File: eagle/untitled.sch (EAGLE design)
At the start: 42 parts, among them J1 JTAG, Q1 16MHz, U1 MMA3202KEG

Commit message: Update board layout.
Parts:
- added D9: (no value), SparkFun-LED:LED1206
- added JP3: (no value), SparkFun-Connectors:M04PTH
- added R14: (no value), SparkFun-Passives:RESISTOR1206
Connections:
- new net N$18: D9.A, R14.2
- new net PB0: JP3.3, U$1.PB0(SS)
- new net PD0: JP3.1, U$1.PD0(SCL)
- new net PD1: JP3.2, U$1.PD1(SDA)
- new net PE6: JP3.4, U$1.PE6
- net GND-ISO: now also D9.C
- net N$28: now also R14.1
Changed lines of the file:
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@@
 <part name="D11" library="gipi" deviceset="DIODE" device=""/>
 <part name="D12" library="gipi" deviceset="DIODE" device=""/>
+<part name="D9" library="SparkFun-LED" deviceset="LED" device="1206"/>
+<part name="R14" library="SparkFun-Passives" deviceset="RESISTOR" device="1206"/>
+<part name="GND-ISO11" library="SparkFun-Aesthetics" deviceset="GND-ISO" device=""/>
+<part name="JP3" library="SparkFun-Connectors" deviceset="M04" device="PTH"/>
 </parts>
 <sheets>
@@
 <instance part="D11" gate="G$1" x="-35.56" y="88.9"/>
 <instance part="D12" gate="G$1" x="185.42" y="40.64"/>
+<instance part="D9" gate="G$1" x="-27.94" y="104.14" rot="R90"/>
+<instance part="R14" gate="G$1" x="-30.48" y="96.52" rot="R90"/>
+<instance part="GND-ISO11" gate="G$1" x="-22.86" y="93.98"/>
+<instance part="JP3" gate="G$1" x="-33.02" y="-40.64"/>
 </instances>
 <busses>
@@
 <pinref part="GND-ISO10" gate="G$1" pin="GND-ISO"/>
 </segment>
+<segment>
+<pinref part="D9" gate="G$1" pin="C"/>
+<wire x1="-22.86" y1="104.14" x2="-22.86" y2="96.52" width="0.1524" layer="91"/>
+<pinref part="GND-ISO11" gate="G$1" pin="GND-ISO"/>
+</segment>
 </net>
 <net name="N$19" class="0">
@@
 <wire x1="-33.02" y1="88.9" x2="-30.48" y2="88.9" width="0.1524" layer="91"/>
 <junction x="-30.48" y="88.9"/>
+<pinref part="R14" gate="G$1" pin="1"/>
+<wire x1="-30.48" y1="88.9" x2="-30.48" y2="91.44" width="0.1524" layer="91"/>
 </segment>
 </net>
@@
 </segment>
 </net>
+<net name="N$18" class="0">
+<segment>
+<pinref part="R14" gate="G$1" pin="2"/>
+<pinref part="D9" gate="G$1" pin="A"/>
+<wire x1="-30.48" y1="101.6" x2="-30.48" y2="104.14" width="0.1524" layer="91"/>
+</segment>
+</net>
+<net name="PB0" class="0">
+<segment>
+<pinref part="U$1" gate="G$1" pin="PB0(SS)"/>
+<wire x1="60.96" y1="20.32" x2="71.12" y2="20.32" width="0.1524" layer="91"/>
+<label x="73.66" y="20.32" size="1.778" layer="95" xref="yes"/>
+</segment>
+<segment>
+<pinref part="JP3" gate="G$1" pin="3"/>
+<wire x1="-27.94" y1="-38.1" x2="-22.86" y2="-38.1" width="0.1524" layer="91"/>
+<label x="-22.86" y="-38.1" size="1.778" layer="95" xref="yes"/>
+</segment>
+</net>
+<net name="PE6" class="0">
+<segment>
+<pinref part="U$1" gate="G$1" pin="PE6"/>
+<wire x1="60.96" y1="38.1" x2="71.12" y2="38.1" width="0.1524" layer="91"/>
+<label x="73.66" y="38.1" size="1.778" layer="95" xref="yes"/>
+</segment>
+<segment>
+<pinref part="JP3" gate="G$1" pin="4"/>
+<wire x1="-27.94" y1="-35.56" x2="-22.86" y2="-35.56" width="0.1524" layer="91"/>
+<label x="-22.86" y="-35.56" size="1.778" layer="95" xref="yes"/>
+</segment>
+</net>
+<net name="PD0" class="0">
+<segment>
+<pinref part="U$1" gate="G$1" pin="PD0(SCL)"/>
+<wire x1="60.96" y1="48.26" x2="71.12" y2="48.26" width="0.1524" layer="91"/>
+<label x="73.66" y="48.26" size="1.778" layer="95" xref="yes"/>
+</segment>
+<segment>
+<pinref part="JP3" gate="G$1" pin="1"/>
+<wire x1="-27.94" y1="-43.18" x2="-22.86" y2="-43.18" width="0.1524" layer="91"/>
+<label x="-22.86" y="-43.18" size="1.778" layer="95" xref="yes"/>
+</segment>
+</net>
+<net name="PD1" class="0">
+<segment>
+<pinref part="U$1" gate="G$1" pin="PD1(SDA)"/>
+<wire x1="60.96" y1="50.8" x2="71.12" y2="50.8" width="0.1524" layer="91"/>
+<label x="73.66" y="50.8" size="1.778" layer="95" xref="yes"/>
+</segment>
+<segment>
+<pinref part="JP3" gate="G$1" pin="2"/>
+<wire x1="-27.94" y1="-40.64" x2="-22.86" y2="-40.64" width="0.1524" layer="91"/>
+<label x="-22.86" y="-40.64" size="1.778" layer="95" xref="yes"/>
+</segment>
+</net>

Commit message: Update eagle.
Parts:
- added U$2: KITTEN, gipi:KITTEN
- G1: device battery:10MM_SM_COIN_CELL_CLIP -> SparkFun-Electromechanical:BATTERY20PTH
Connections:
- net GND-ISO: now also G1.+; no longer G1.-
- net N$33: now also G1.-; no longer G1.+
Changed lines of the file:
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@@
 <part name="C2" library="SparkFun-Capacitors" deviceset="CAP" device="1206"/>
 <part name="U1" library="gipi" deviceset="MMA3202KEG" device=""/>
-<part name="G1" library="battery" deviceset="10MM_SM_COIN_CELL_CLIP" device="" value="BAT"/>
+<part name="G1" library="SparkFun-Electromechanical" deviceset="BATTERY" device="20PTH" value="BAT"/>
 <part name="GND-ISO4" library="SparkFun-Aesthetics" deviceset="GND-ISO" device=""/>
 <part name="C3" library="SparkFun-Capacitors" deviceset="CAP" device="1206"/>
@@
 <part name="GND-ISO11" library="SparkFun-Aesthetics" deviceset="GND-ISO" device=""/>
 <part name="JP3" library="SparkFun-Connectors" deviceset="M04" device="PTH"/>
+<part name="U$2" library="gipi" deviceset="KITTEN" device=""/>
 </parts>
 <sheets>
@@
 </segment>
 <segment>
-<pinref part="G1" gate="G$1" pin="-"/>
+<pinref part="G1" gate="G$1" pin="+"/>
 <wire x1="-40.64" y1="78.74" x2="-40.64" y2="68.58" width="0.1524" layer="91"/>
 <pinref part="GND-ISO5" gate="G$1" pin="GND-ISO"/>
@@
 <net name="N$33" class="0">
 <segment>
-<pinref part="G1" gate="G$1" pin="+"/>
+<pinref part="G1" gate="G$1" pin="-"/>
 <pinref part="D11" gate="G$1" pin="A"/>
 <wire x1="-40.64" y1="88.9" x2="-38.1" y2="88.9" width="0.1524" layer="91"/>

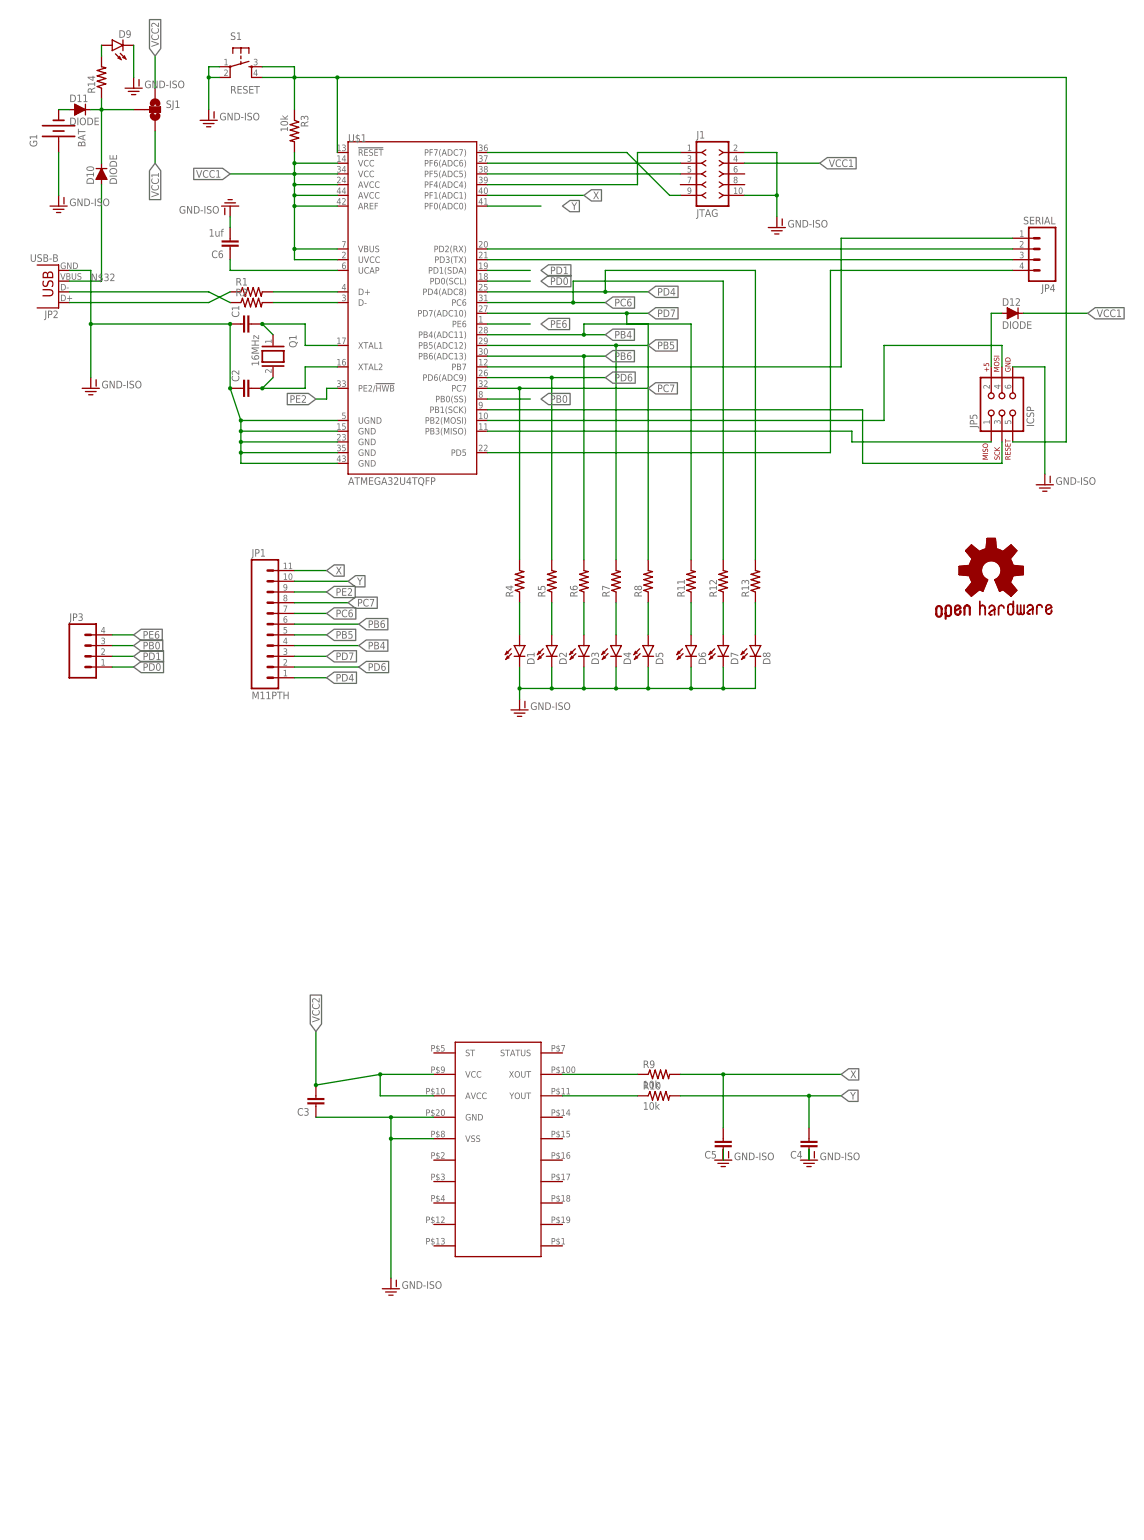
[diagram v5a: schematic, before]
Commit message: Update some component values.
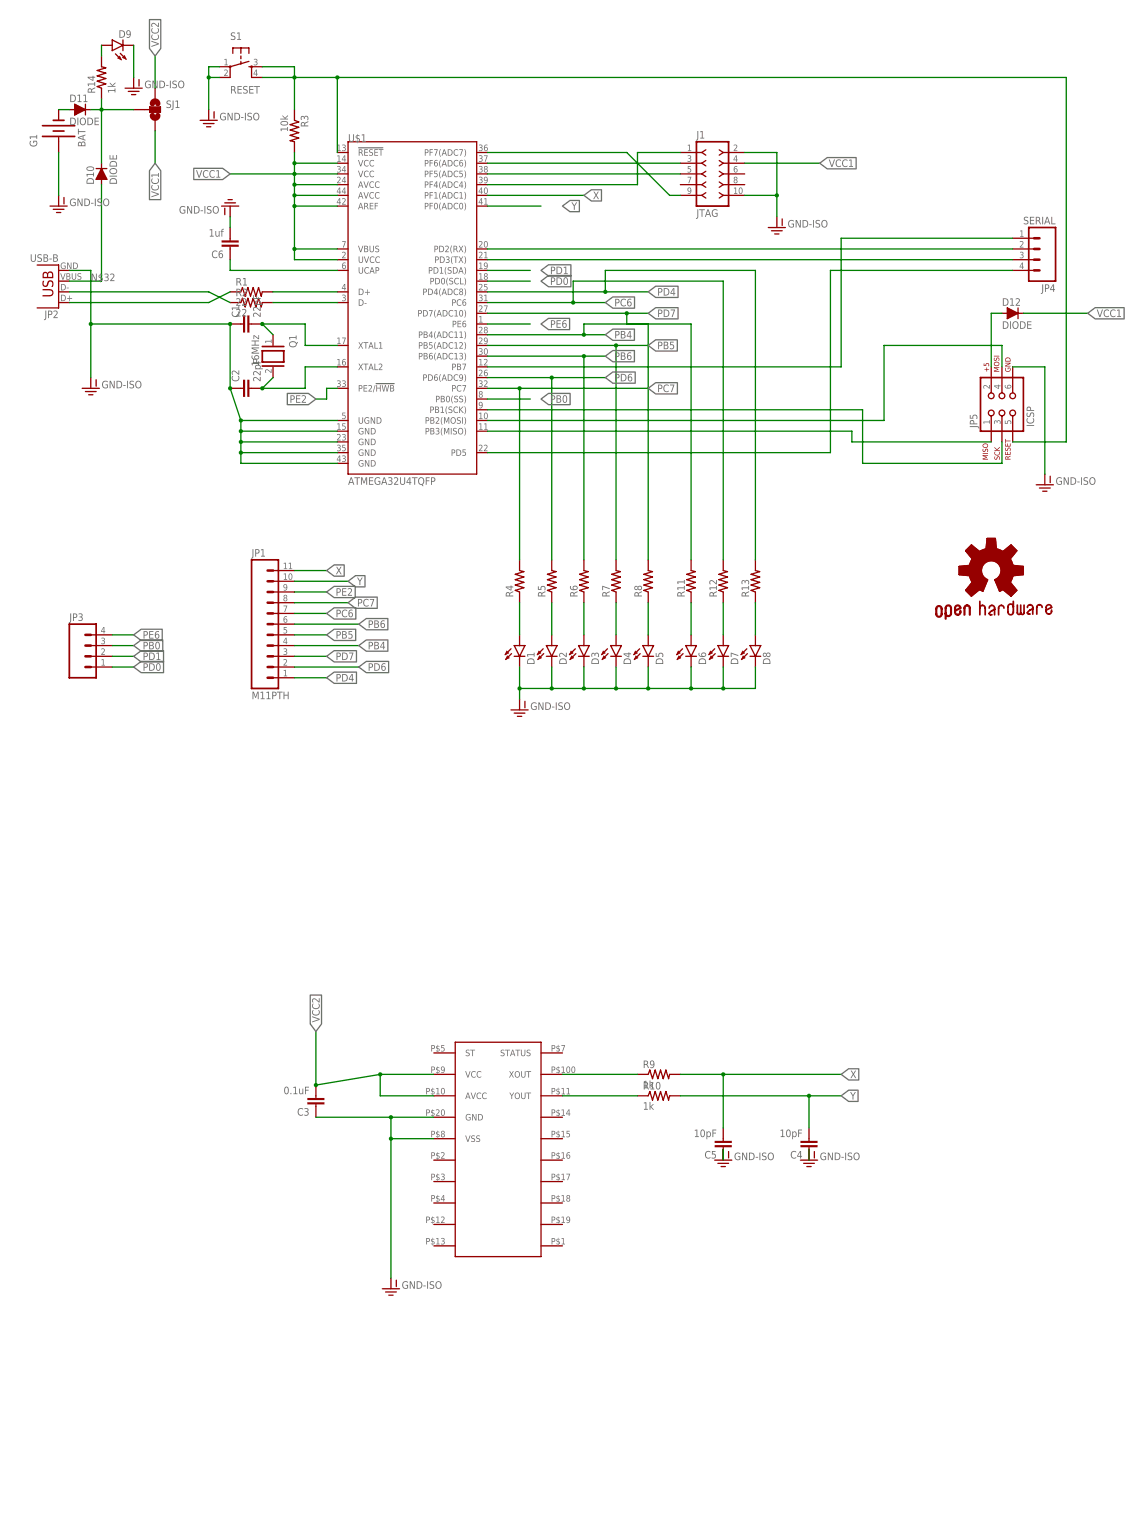
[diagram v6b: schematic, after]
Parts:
- removed U$2: KITTEN, gipi:KITTEN
- C1, C2: value (none) -> 22pF
- C3: value (none) -> 0.1uF
- C4, C5: value (none) -> 10pF
- R1, R2: value (none) -> 22
- R10, R9: value 10k -> 1k
- R14: value (none) -> 1k
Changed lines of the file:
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@@
 <parts>
 <part name="U$1" library="SparkFun-Retired" deviceset="ATMEGA32U4" device="TQFP"/>
-<part name="R1" library="SparkFun-Passives" deviceset="RESISTOR" device="1206"/>
-<part name="R2" library="SparkFun-Passives" deviceset="RESISTOR" device="1206"/>
+<part name="R1" library="SparkFun-Passives" deviceset="RESISTOR" device="1206" value="22"/>
+<part name="R2" library="SparkFun-Passives" deviceset="RESISTOR" device="1206" value="22"/>
 <part name="S1" library="SparkFun-Retired" deviceset="TAC_SWITCH" device="SMD" value="RESET"/>
 <part name="R3" library="SparkFun-Passives" deviceset="RESISTOR" device="1206" value="10k"/>
@@
 <part name="GND-ISO2" library="SparkFun-Aesthetics" deviceset="GND-ISO" device=""/>
 <part name="Q1" library="special" deviceset="XTAL/S" device="" value="16MHz"/>
-<part name="C1" library="SparkFun-Capacitors" deviceset="CAP" device="1206"/>
-<part name="C2" library="SparkFun-Capacitors" deviceset="CAP" device="1206"/>
+<part name="C1" library="SparkFun-Capacitors" deviceset="CAP" device="1206" value="22pF"/>
+<part name="C2" library="SparkFun-Capacitors" deviceset="CAP" device="1206" value="22pF"/>
 <part name="U1" library="gipi" deviceset="MMA3202KEG" device=""/>
 <part name="G1" library="SparkFun-Electromechanical" deviceset="BATTERY" device="20PTH" value="BAT"/>
 <part name="GND-ISO4" library="SparkFun-Aesthetics" deviceset="GND-ISO" device=""/>
-<part name="C3" library="SparkFun-Capacitors" deviceset="CAP" device="1206"/>
+<part name="C3" library="SparkFun-Capacitors" deviceset="CAP" device="1206" value="0.1uF"/>
 <part name="SJ1" library="SparkFun-Retired" deviceset="SOLDERJUMPER_2WAY" device="PASTE2&amp;3"/>
 <part name="GND-ISO5" library="SparkFun-Aesthetics" deviceset="GND-ISO" device=""/>
-<part name="R9" library="SparkFun-Passives" deviceset="RESISTOR" device="1206" value="10k"/>
-<part name="R10" library="SparkFun-Passives" deviceset="RESISTOR" device="1206" value="10k"/>
-<part name="C4" library="SparkFun-Capacitors" deviceset="CAP" device="1206"/>
-<part name="C5" library="SparkFun-Capacitors" deviceset="CAP" device="1206"/>
+<part name="R9" library="SparkFun-Passives" deviceset="RESISTOR" device="1206" value="1k"/>
+<part name="R10" library="SparkFun-Passives" deviceset="RESISTOR" device="1206" value="1k"/>
+<part name="C4" library="SparkFun-Capacitors" deviceset="CAP" device="1206" value="10pF"/>
+<part name="C5" library="SparkFun-Capacitors" deviceset="CAP" device="1206" value="10pF"/>
 <part name="GND-ISO6" library="SparkFun-Aesthetics" deviceset="GND-ISO" device=""/>
 <part name="GND-ISO7" library="SparkFun-Aesthetics" deviceset="GND-ISO" device=""/>
@@
 <part name="D12" library="gipi" deviceset="DIODE" device=""/>
 <part name="D9" library="SparkFun-LED" deviceset="LED" device="1206"/>
-<part name="R14" library="SparkFun-Passives" deviceset="RESISTOR" device="1206"/>
+<part name="R14" library="SparkFun-Passives" deviceset="RESISTOR" device="1206" value="1k"/>
 <part name="GND-ISO11" library="SparkFun-Aesthetics" deviceset="GND-ISO" device=""/>
 <part name="JP3" library="SparkFun-Connectors" deviceset="M04" device="PTH"/>
-<part name="U$2" library="gipi" deviceset="KITTEN" device=""/>
 </parts>
 <sheets>

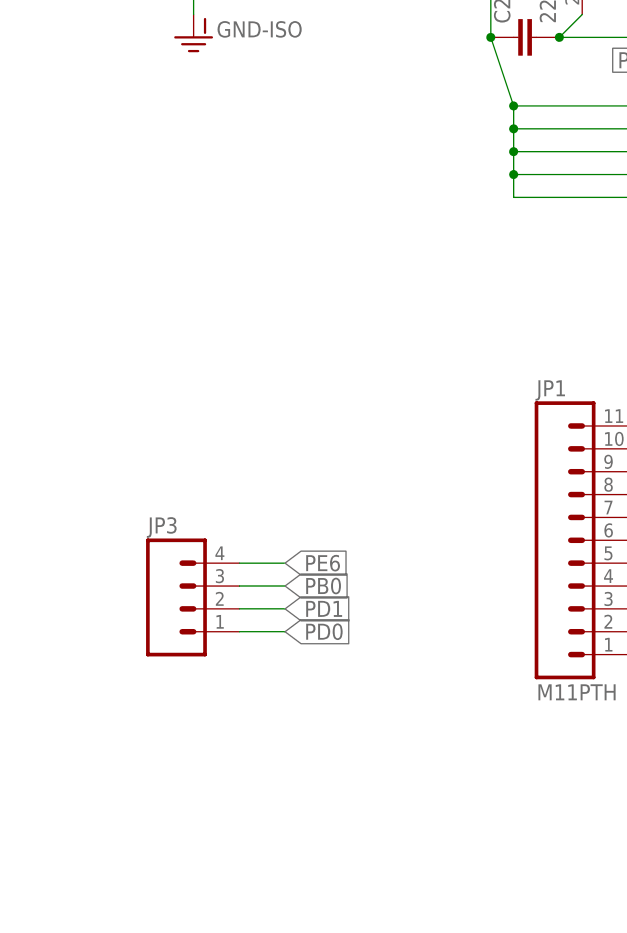
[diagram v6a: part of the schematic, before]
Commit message: Add BOOT button and reroute stuffs.
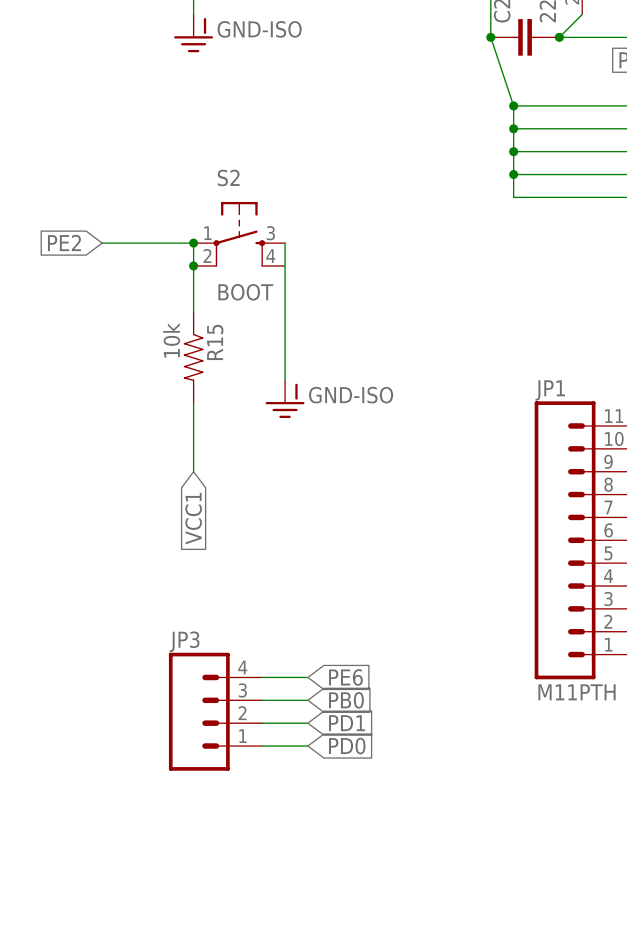
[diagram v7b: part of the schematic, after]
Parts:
- added R15: 10k, SparkFun-Passives:RESISTOR1206
- added S2: BOOT, SparkFun-Retired:TAC_SWITCHSMD
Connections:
- net GND-ISO: now also S2.3
- net PE2: now also R15.1, S2.1, S2.2
- net VCC1: now also R15.2
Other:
- moved on the sheet: JP3
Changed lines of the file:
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@@
 <part name="GND-ISO11" library="SparkFun-Aesthetics" deviceset="GND-ISO" device=""/>
 <part name="JP3" library="SparkFun-Connectors" deviceset="M04" device="PTH"/>
+<part name="S2" library="SparkFun-Retired" deviceset="TAC_SWITCH" device="SMD" value="BOOT"/>
+<part name="GND-ISO12" library="SparkFun-Aesthetics" deviceset="GND-ISO" device=""/>
+<part name="R15" library="SparkFun-Passives" deviceset="RESISTOR" device="1206" value="10k"/>
 </parts>
 <sheets>
@@
 <instance part="R14" gate="G$1" x="-30.48" y="96.52" rot="R90"/>
 <instance part="GND-ISO11" gate="G$1" x="-22.86" y="93.98"/>
-<instance part="JP3" gate="G$1" x="-33.02" y="-40.64"/>
+<instance part="JP3" gate="G$1" x="-30.48" y="-53.34"/>
+<instance part="S2" gate="S" x="-27.94" y="0"/>
+<instance part="GND-ISO12" gate="G$1" x="-22.86" y="-17.78"/>
+<instance part="R15" gate="G$1" x="-33.02" y="-12.7" rot="R270"/>
 </instances>
 <busses>
@@
 <pinref part="GND-ISO11" gate="G$1" pin="GND-ISO"/>
 </segment>
+<segment>
+<pinref part="S2" gate="S" pin="3"/>
+<pinref part="GND-ISO12" gate="G$1" pin="GND-ISO"/>
+<wire x1="-22.86" y1="0" x2="-22.86" y2="-15.24" width="0.1524" layer="91"/>
+</segment>
 </net>
 <net name="N$19" class="0">
@@
 <label x="203.2" y="40.64" size="1.778" layer="95" xref="yes"/>
 </segment>
+<segment>
+<pinref part="R15" gate="G$1" pin="2"/>
+<wire x1="-33.02" y1="-17.78" x2="-33.02" y2="-25.4" width="0.1524" layer="91"/>
+<label x="-33.02" y="-25.4" size="1.778" layer="95" rot="R270" xref="yes"/>
+</segment>
 </net>
 <net name="VCC2" class="0">
@@
 <label x="20.32" y="20.32" size="1.778" layer="95" rot="R180" xref="yes"/>
 </segment>
+<segment>
+<pinref part="S2" gate="S" pin="1"/>
+<wire x1="-33.02" y1="0" x2="-43.18" y2="0" width="0.1524" layer="91"/>
+<label x="-43.18" y="0" size="1.778" layer="95" rot="R180" xref="yes"/>
+<pinref part="S2" gate="S" pin="2"/>
+<pinref part="R15" gate="G$1" pin="1"/>
+<wire x1="-33.02" y1="-2.54" x2="-33.02" y2="-7.62" width="0.1524" layer="91"/>
+<wire x1="-33.02" y1="-2.54" x2="-33.02" y2="0" width="0.1524" layer="91"/>
+<junction x="-33.02" y="-2.54"/>
+<junction x="-33.02" y="0"/>
+</segment>
 </net>
 <net name="N$2" class="0">
@@
 <segment>
 <pinref part="JP3" gate="G$1" pin="3"/>
-<wire x1="-27.94" y1="-38.1" x2="-22.86" y2="-38.1" width="0.1524" layer="91"/>
-<label x="-22.86" y="-38.1" size="1.778" layer="95" xref="yes"/>
+<wire x1="-25.4" y1="-50.8" x2="-20.32" y2="-50.8" width="0.1524" layer="91"/>
+<label x="-20.32" y="-50.8" size="1.778" layer="95" xref="yes"/>
 </segment>
 </net>
@@
 <segment>
 <pinref part="JP3" gate="G$1" pin="4"/>
-<wire x1="-27.94" y1="-35.56" x2="-22.86" y2="-35.56" width="0.1524" layer="91"/>
-<label x="-22.86" y="-35.56" size="1.778" layer="95" xref="yes"/>
+<wire x1="-25.4" y1="-48.26" x2="-20.32" y2="-48.26" width="0.1524" layer="91"/>
+<label x="-20.32" y="-48.26" size="1.778" layer="95" xref="yes"/>
 </segment>
 </net>
@@
 <segment>
 <pinref part="JP3" gate="G$1" pin="1"/>
-<wire x1="-27.94" y1="-43.18" x2="-22.86" y2="-43.18" width="0.1524" layer="91"/>
-<label x="-22.86" y="-43.18" size="1.778" layer="95" xref="yes"/>
+<wire x1="-25.4" y1="-55.88" x2="-20.32" y2="-55.88" width="0.1524" layer="91"/>
+<label x="-20.32" y="-55.88" size="1.778" layer="95" xref="yes"/>
 </segment>
 </net>
@@
 <segment>
 <pinref part="JP3" gate="G$1" pin="2"/>
-<wire x1="-27.94" y1="-40.64" x2="-22.86" y2="-40.64" width="0.1524" layer="91"/>
-<label x="-22.86" y="-40.64" size="1.778" layer="95" xref="yes"/>
-</segment>
-</net>
+<wire x1="-25.4" y1="-53.34" x2="-20.32" y2="-53.34" width="0.1524" layer="91"/>
+<label x="-20.32" y="-53.34" size="1.778" layer="95" xref="yes"/>
+</segment>
+</net>
